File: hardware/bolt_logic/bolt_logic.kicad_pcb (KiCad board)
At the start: 2 copper layers, 289 x 112 mm, 16 parts, among them CN1 GM X1 48-way, CN2 B2B 2x20 2.54mm

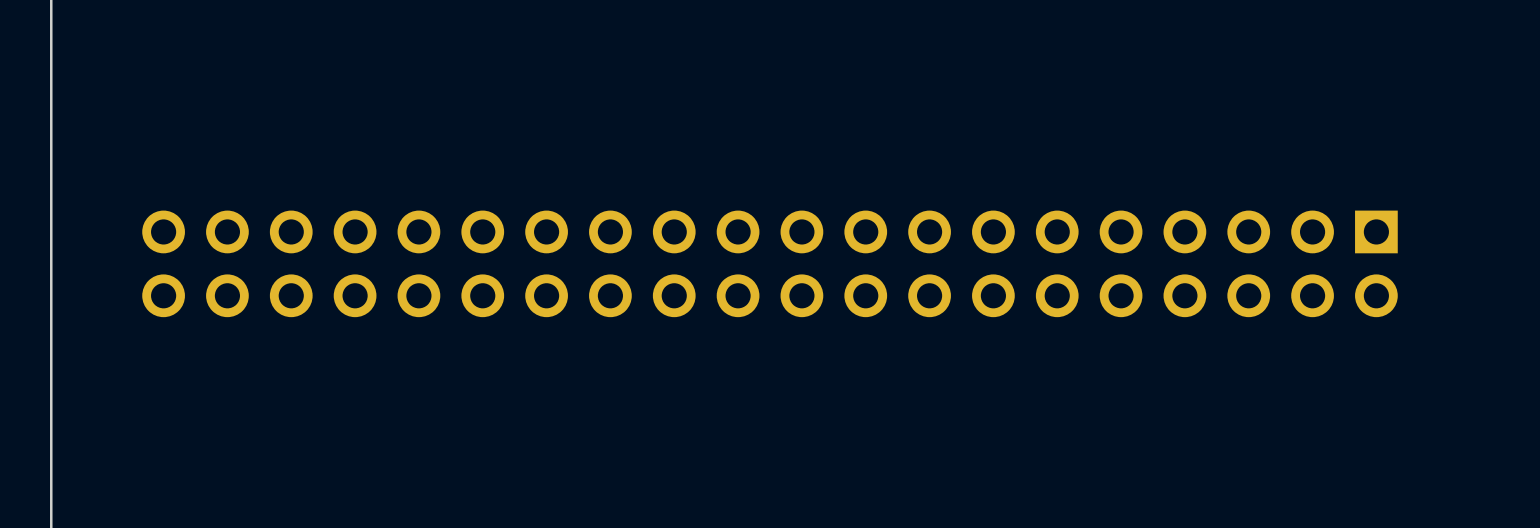
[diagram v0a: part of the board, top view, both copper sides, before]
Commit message: Add schematic design spec; identify CN2 as Samtec SSW-120-01-T-D-LL
docs/03-schematic-design.md: block-by-block design from a full read of the
Tesla V6 schematic - HW_BOLT STM32 pin map, reuse/adapt/new/drop per block
with values, CN1/CN2 net assignments, CN1 vehicle-pinout proposal,
software-resolver front end, firmware change list, open questions.

CN2 footprint: 1.02 mm drill for Samtec SSW (0.64 mm square tails).
Architecture doc corrected: the V6 hardware is encoder-only (resolver is
new design) and current gain is 2.25 digits/A with the V6's 2k7/4k7 divider.

Co-Authored-By: Claude Opus 5.5 <noreply@anthropic.com>
Claude-Session: https://claude.ai/code/session_01KW1M8KfVLc83FDDiK2YEWM
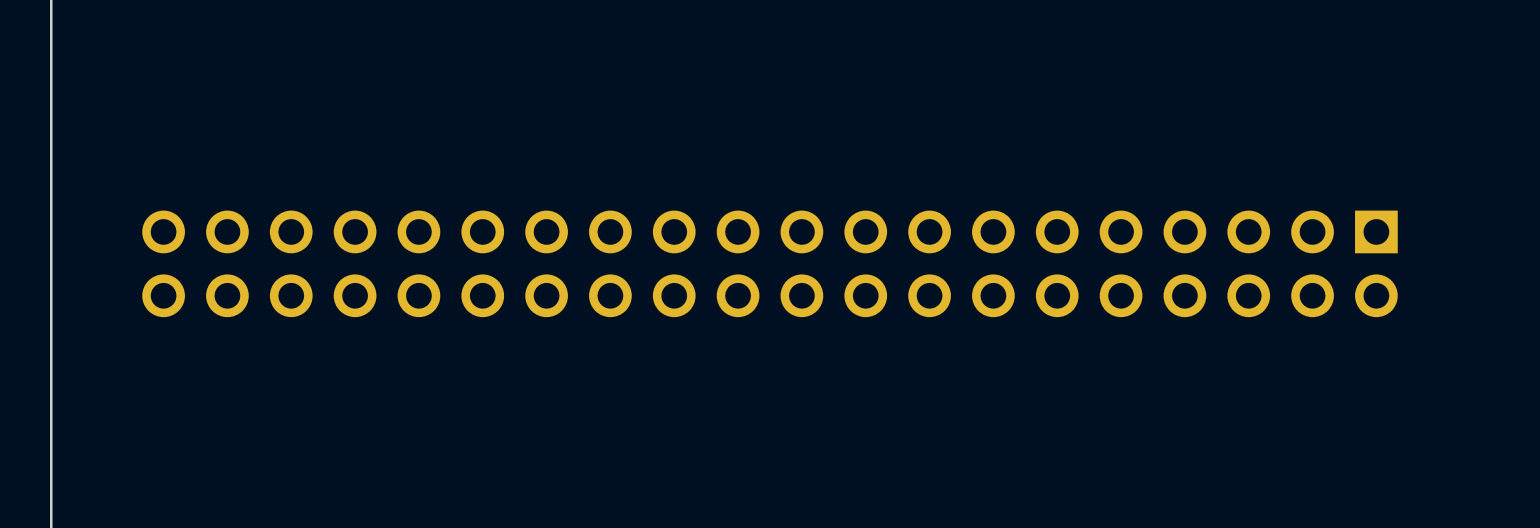
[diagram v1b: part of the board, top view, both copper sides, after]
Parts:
- CN2: value B2B 2x20 2.54mm -> SSW-120-01-T-D-LL

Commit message: PCB layout v0.1: scripted placement and autorouting, DRC clean
- gen_layout.py: footprints from the KiCad netlist with a pad-by-pad
  cross-check, grouped placement by function, decoupling caps placed at
  their pins, 2-pin parts rotated so each pad faces its own net.
- gen_route.py: 4-layer stackup (In1 solid GND), pre-routed short pad
  pairs, GND fan-out before routing, FreeRouting via DSN/SES with a
  custom SES importer (KiCad 7 import needs the GUI), dangling cleanup,
  direct completion of leftover connections, GND stitching, pours with
  orphan-island vias, DRC and a routed render.
- Net class widths are capped below the narrowest SMD pad on each net
  (FreeRouting cannot neck down into fine-pitch pins).
- Result: 0 clearance/short violations, 0 unconnected items; 17 silk
  warnings remain for the hand-review pass.
- gen_mech.py keeps footprint files unchanged when only tstamps differ.
- docs/04-layout.md: flow, results and the hand-review list before fab.

Co-Authored-By: Claude Opus 5.5 <noreply@anthropic.com>
Claude-Session: https://claude.ai/code/session_01KW1M8KfVLc83FDDiK2YEWM
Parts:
- added C1: 10uF 50V, Capacitor_SMD:C_1206_3216Metric, F.Cu at (85.2, 111.9)
- added C10: 10uF, Capacitor_SMD:C_1206_3216Metric, F.Cu at (105.1, 122.8)
- added C100: 1uF, Capacitor_SMD:C_0805_2012Metric, F.Cu at (137.2, 147.0)
- added C101: 1uF, Capacitor_SMD:C_0805_2012Metric, F.Cu at (140.3, 151.5)
- added C102: 1uF, Capacitor_SMD:C_0805_2012Metric, F.Cu at (98.8, 133.0)
- added C103: 1uF, Capacitor_SMD:C_0805_2012Metric, F.Cu at (140.3, 147.8)
- added C104: 1uF, Capacitor_SMD:C_0805_2012Metric, F.Cu at (130.5, 140.3)
- added C105: 100nF, Capacitor_SMD:C_0805_2012Metric, F.Cu at (150.0, 150.0)
- added C106: 100nF, Capacitor_SMD:C_0805_2012Metric, F.Cu at (145.5, 150.0)
- added C107: 1uF, Capacitor_SMD:C_0805_2012Metric, F.Cu at (107.0, 136.0)
- added C108: 1uF, Capacitor_SMD:C_0805_2012Metric, F.Cu at (135.0, 143.3)
- added C109: 100nF, Capacitor_SMD:C_0805_2012Metric, F.Cu at (82.7, 136.0)
- added C11: 22uF, Capacitor_SMD:C_1206_3216Metric, F.Cu at (105.1, 119.8)
- added C12: 100nF, Capacitor_SMD:C_0805_2012Metric, F.Cu at (106.0, 117.0)
- added C120: 10uF, Capacitor_SMD:C_1206_3216Metric, F.Cu at (325.4, 161.4)
- added C121: 100nF, Capacitor_SMD:C_0805_2012Metric, F.Cu at (328.2, 165.7)
- added C122: 100nF, Capacitor_SMD:C_0805_2012Metric, F.Cu at (321.5, 159.8)
- added C13: 10uF, Capacitor_SMD:C_1206_3216Metric, F.Cu at (98.3, 120.6)
- added C14: 100nF, Capacitor_SMD:C_0805_2012Metric, F.Cu at (94.8, 111.8)
- added C15: 10uF 25V, Capacitor_SMD:C_1206_3216Metric, F.Cu at (75.4, 105.2)
- added C16: 100nF, Capacitor_SMD:C_0805_2012Metric, F.Cu at (82.8, 104.3)
- added C2: 10uF 50V, Capacitor_SMD:C_1206_3216Metric, F.Cu at (88.2, 111.9)
- added C20: 100nF, Capacitor_SMD:C_0805_2012Metric, F.Cu at (145.5, 183.8)
- added C21: 100nF, Capacitor_SMD:C_0805_2012Metric, F.Cu at (152.3, 183.8)
- added C22: 100nF, Capacitor_SMD:C_0805_2012Metric, F.Cu at (159.7, 171.0)
- added C23: 100nF, Capacitor_SMD:C_0805_2012Metric, F.Cu at (139.5, 169.5)
- added C24: 4.7uF, Capacitor_SMD:C_0805_2012Metric, F.Cu at (136.5, 168.7)
- added C25: 1uF, Capacitor_SMD:C_0805_2012Metric, F.Cu at (139.5, 182.3)
- added C26: 100nF, Capacitor_SMD:C_0805_2012Metric, F.Cu at (136.5, 178.5)
- added C27: 100nF, Capacitor_SMD:C_0805_2012Metric, F.Cu at (142.5, 183.8)
- added C28: 22pF, Capacitor_SMD:C_0805_2012Metric, F.Cu at (132.0, 171.7)
- added C29: 22pF, Capacitor_SMD:C_0805_2012Metric, F.Cu at (132.0, 175.5)
- added C3: 10uF 50V, Capacitor_SMD:C_1206_3216Metric, F.Cu at (79.9, 105.2)
- added C30: 10pF, Capacitor_SMD:C_0805_2012Metric, F.Cu at (136.5, 181.5)
- added C31: 10pF, Capacitor_SMD:C_0805_2012Metric, F.Cu at (139.5, 186.0)
- added C4: 10uF 50V, Capacitor_SMD:C_1206_3216Metric, F.Cu at (84.1, 107.8)
- added C40: 100nF, Capacitor_SMD:C_0805_2012Metric, F.Cu at (106.7, 170.2)
- added C41: 10nF, Capacitor_SMD:C_0805_2012Metric, F.Cu at (109.0, 174.8)
- added C42: 10nF, Capacitor_SMD:C_0805_2012Metric, F.Cu at (110.5, 171.7)
- added C43: 10nF, Capacitor_SMD:C_0805_2012Metric, F.Cu at (102.2, 176.2)
- added C44: 10nF, Capacitor_SMD:C_0805_2012Metric, F.Cu at (106.0, 173.2)
- added C45: 10nF, Capacitor_SMD:C_0805_2012Metric, F.Cu at (111.0, 195.3)
- added C46: 100nF, Capacitor_SMD:C_0805_2012Metric, F.Cu at (110.5, 168.0)
- added C47: 100nF, Capacitor_SMD:C_0805_2012Metric, F.Cu at (110.5, 165.0)
- added C48: 1nF, Capacitor_SMD:C_0805_2012Metric, F.Cu at (124.8, 162.0)
- added C5: 100nF, Capacitor_SMD:C_0805_2012Metric, F.Cu at (91.7, 113.2)
- added C50: 4.7nF, Capacitor_SMD:C_0805_2012Metric, F.Cu at (80.8, 196.0)
- added C51: 1nF, Capacitor_SMD:C_0805_2012Metric, F.Cu at (75.5, 177.7)
- added C52: 4.7nF, Capacitor_SMD:C_0805_2012Metric, F.Cu at (84.5, 191.5)
- added C53: 1nF, Capacitor_SMD:C_0805_2012Metric, F.Cu at (75.5, 172.5)
- added C54: 100nF, Capacitor_SMD:C_0805_2012Metric, F.Cu at (74.8, 199.8)
- added C55: 4.7nF, Capacitor_SMD:C_0805_2012Metric, F.Cu at (69.5, 200.5)
- added C56: 1nF, Capacitor_SMD:C_0805_2012Metric, F.Cu at (71.0, 174.7)
- added C57: 100nF, Capacitor_SMD:C_0805_2012Metric, F.Cu at (66.5, 198.3)
- added C58: 1uF, Capacitor_SMD:C_0805_2012Metric, F.Cu at (89.0, 162.0)
- added C59: 1uF, Capacitor_SMD:C_0805_2012Metric, F.Cu at (83.0, 160.5)
- added C6: 100nF, Capacitor_SMD:C_0805_2012Metric, F.Cu at (94.0, 118.5)
- added C60: 100nF, Capacitor_SMD:C_0805_2012Metric, F.Cu at (69.5, 162.7)
- added C61: 100nF, Capacitor_SMD:C_0805_2012Metric, F.Cu at (67.2, 166.5)
- added C62: 100nF, Capacitor_SMD:C_0805_2012Metric, F.Cu at (88.3, 192.3)
- added C63: 1uF, Capacitor_SMD:C_0805_2012Metric, F.Cu at (71.7, 165.7)
- added C64: 1uF, Capacitor_SMD:C_0805_2012Metric, F.Cu at (69.5, 169.5)
- added C65: 1uF, Capacitor_SMD:C_0805_2012Metric, F.Cu at (71.8, 177.8)
- added C66: 1uF, Capacitor_SMD:C_0805_2012Metric, F.Cu at (78.5, 160.5)
- added C67: 1uF, Capacitor_SMD:C_0805_2012Metric, F.Cu at (74.0, 161.2)
- added C7: 22uF, Capacitor_SMD:C_1206_3216Metric, F.Cu at (96.1, 115.3)
- added C70: 3.3nF, Capacitor_SMD:C_0805_2012Metric, F.Cu at (111.3, 154.0)
- added C71: 4.7nF, Capacitor_SMD:C_0805_2012Metric, F.Cu at (88.0, 157.0)
- added C72: 2.2nF, Capacitor_SMD:C_0805_2012Metric, F.Cu at (95.5, 154.0)
- added C73: 100nF, Capacitor_SMD:C_0805_2012Metric, F.Cu at (76.0, 142.0)
- added C75: 100nF, Capacitor_SMD:C_0805_2012Metric, F.Cu at (103.7, 155.5)
- added C76: 1uF, Capacitor_SMD:C_0805_2012Metric, F.Cu at (94.8, 150.3)
- added C77: 10uF 25V, Capacitor_SMD:C_1206_3216Metric, F.Cu at (96.8, 144.1)
- added C78: 10uF 25V, Capacitor_SMD:C_1206_3216Metric, F.Cu at (98.3, 139.6)
- added C79: 100nF, Capacitor_SMD:C_0805_2012Metric, F.Cu at (103.0, 142.0)
- added C8: 22uF, Capacitor_SMD:C_1206_3216Metric, F.Cu at (91.2, 108.9)
- added C80: 10uF 25V, Capacitor_SMD:C_1206_3216Metric, F.Cu at (103.6, 138.8)
- added C81: 10uF 25V, Capacitor_SMD:C_1206_3216Metric, F.Cu at (97.9, 148.2)
- added C82: 1nF, Capacitor_SMD:C_0805_2012Metric, F.Cu at (75.2, 139.0)
- added C83: 1nF, Capacitor_SMD:C_0805_2012Metric, F.Cu at (96.2, 157.0)
- added C84: 100nF, Capacitor_SMD:C_0805_2012Metric, F.Cu at (105.2, 149.5)
- added C85: 1nF, Capacitor_SMD:C_0805_2012Metric, F.Cu at (99.2, 152.5)
- added C86: 1nF, Capacitor_SMD:C_0805_2012Metric, F.Cu at (100.0, 155.5)
- added C87: 1nF, Capacitor_SMD:C_0805_2012Metric, F.Cu at (101.5, 149.5)
- added C88: 1nF, Capacitor_SMD:C_0805_2012Metric, F.Cu at (101.5, 145.0)
- added C89: 1nF, Capacitor_SMD:C_0805_2012Metric, F.Cu at (103.0, 152.5)
- added C9: 100nF, Capacitor_SMD:C_0805_2012Metric, F.Cu at (88.0, 107.3)
- added D1: SS54, Diode_SMD:D_SMA, F.Cu at (77.8, 110.2)
- added D2: BAT54S, Package_TO_SOT_SMD:SOT-23, F.Cu at (124.2, 168.6)
- added F1: 50mA, Fuse:Fuse_1206_3216Metric, F.Cu at (95.1, 130.2)
- added F2: 200mA, Fuse:Fuse_1206_3216Metric, F.Cu at (96.3, 126.1)
- added F3: 100mA, Fuse:Fuse_1206_3216Metric, F.Cu at (101.6, 126.1)
- added F4: 500mA, Fuse:Fuse_1812_4532Metric, F.Cu at (208.7, 104.0)
- added FB1: 600R@100MHz 1A, Inductor_SMD:L_0805_2012Metric, F.Cu at (86.5, 123.1)
- added J1: SWD, Connector_PinHeader_2.54mm:PinHeader_1x05_P2.54mm_Vertical, F.Cu at (145.6, 165.7)
- added J3: AUX I/O, Connector_PinHeader_2.54mm:PinHeader_2x06_P2.54mm_Vertical, F.Cu at (201.8, 101.5)
- added J4: ESP PROG, Connector_PinHeader_2.54mm:PinHeader_1x06_P2.54mm_Vertical, F.Cu at (307.3, 185.9)
- added L1: 6.8uH, Inductor_SMD:L_Bourns_SRN6045TA, F.Cu at (88.8, 118.2)
- added L2: 10uH, Inductor_SMD:L_0805_2012Metric, F.Cu at (139.4, 174.0)
- added L30: 10uH, Inductor_SMD:L_0805_2012Metric, F.Cu at (293.8, 167.4)
- added LED1: PWR green, LED_SMD:LED_0805_2012Metric, F.Cu at (156.8, 176.3)
- added LED2: STATUS, LED_SMD:LED_0805_2012Metric, F.Cu at (150.0, 161.3)
- added Q1: BTS443P, Package_TO_SOT_SMD:TO-252-4, F.Cu at (69.5, 117.6)
- added Q2: BTS443P, Package_TO_SOT_SMD:TO-252-4, F.Cu at (77.0, 117.6)
- added R1: 10k, Resistor_SMD:R_0805_2012Metric, F.Cu at (67.0, 110.3)
- added R10: 10k, Resistor_SMD:R_0805_2012Metric, F.Cu at (141.7, 166.5)
- added R100: 4.7k, Resistor_SMD:R_0805_2012Metric, F.Cu at (129.7, 153.0)
- added R101: 1.5k, Resistor_SMD:R_0805_2012Metric, F.Cu at (130.5, 150.0)
- added R102: 4.7k, Resistor_SMD:R_0805_2012Metric, F.Cu at (133.5, 153.0)
- added R103: 1.5k, Resistor_SMD:R_0805_2012Metric, F.Cu at (134.2, 150.0)
- added R104: 4.7k, Resistor_SMD:R_0805_2012Metric, F.Cu at (95.7, 136.0)
- added R105: 1.5k, Resistor_SMD:R_0805_2012Metric, F.Cu at (99.5, 136.0)
- added R106: 4.7k, Resistor_SMD:R_0805_2012Metric, F.Cu at (137.2, 153.0)
- added R107: 1.5k, Resistor_SMD:R_0805_2012Metric, F.Cu at (138.0, 150.0)
- added R108: 4.7k, Resistor_SMD:R_0805_2012Metric, F.Cu at (129.7, 147.0)
- added R109: 1.5k, Resistor_SMD:R_0805_2012Metric, F.Cu at (130.5, 144.0)
- added R11: 4.7k, Resistor_SMD:R_0805_2012Metric, F.Cu at (150.0, 183.8)
- added R110: 1k, Resistor_SMD:R_0805_2012Metric, F.Cu at (153.0, 152.3)
- added R111: 10k, Resistor_SMD:R_0805_2012Metric, F.Cu at (150.0, 153.0)
- added R112: 1k, Resistor_SMD:R_0805_2012Metric, F.Cu at (143.2, 152.3)
- added R113: 10k, Resistor_SMD:R_0805_2012Metric, F.Cu at (146.2, 153.0)
- added R114: 10k, Resistor_SMD:R_0805_2012Metric, F.Cu at (103.2, 136.0)
- added R115: 10k, Resistor_SMD:R_0805_2012Metric, F.Cu at (102.5, 133.0)
- added R116: 10k, Resistor_SMD:R_0805_2012Metric, F.Cu at (133.5, 147.0)
- added R117: 10k, Resistor_SMD:R_0805_2012Metric, F.Cu at (132.7, 144.0)
- added R12: 470, Resistor_SMD:R_0805_2012Metric, F.Cu at (156.7, 171.8)
- added R120: 10k, Resistor_SMD:R_0805_2012Metric, F.Cu at (130.0, 99.0)
- added R121: 10k, Resistor_SMD:R_0805_2012Metric, F.Cu at (142.0, 99.0)
- added R122: 10k, Resistor_SMD:R_0805_2012Metric, F.Cu at (163.7, 114.8)
- added R123: 120, Resistor_SMD:R_0805_2012Metric, F.Cu at (77.5, 127.0)
- added R124: 0R, Resistor_SMD:R_0805_2012Metric, F.Cu at (80.5, 127.0)
- added R13: 1k, Resistor_SMD:R_0805_2012Metric, F.Cu at (147.7, 161.3)
- added R130: 4.7k, Resistor_SMD:R_0805_2012Metric, F.Cu at (322.2, 162.8)
- added R14: 10k, Resistor_SMD:R_0805_2012Metric, F.Cu at (142.5, 163.5)
- added R2: 6.8k, Resistor_SMD:R_0805_2012Metric, F.Cu at (67.0, 106.5)
- added R20: 124k, Resistor_SMD:R_0805_2012Metric, F.Cu at (97.0, 164.3)
- added R21: 100k, Resistor_SMD:R_0805_2012Metric, F.Cu at (97.7, 180.0)
- added R22: 560, Resistor_SMD:R_0805_2012Metric, F.Cu at (106.0, 175.5)
- added R23: 100k, Resistor_SMD:R_0805_2012Metric, F.Cu at (100.7, 179.3)
- added R24: 560, Resistor_SMD:R_0805_2012Metric, F.Cu at (109.0, 180.0)
- added R25: 100k, Resistor_SMD:R_0805_2012Metric, F.Cu at (105.7, 191.5)
- added R26: 560, Resistor_SMD:R_0805_2012Metric, F.Cu at (105.2, 180.0)
- added R27: 100k, Resistor_SMD:R_0805_2012Metric, F.Cu at (97.7, 177.0)
- added R28: 560, Resistor_SMD:R_0805_2012Metric, F.Cu at (106.7, 177.8)
- added R29: 100k, Resistor_SMD:R_0805_2012Metric, F.Cu at (105.7, 193.8)
- added R3: 1k, Resistor_SMD:R_0805_2012Metric, F.Cu at (82.7, 122.3)
- added R30: 560, Resistor_SMD:R_0805_2012Metric, F.Cu at (108.7, 192.3)
- added R31: 10k, Resistor_SMD:R_0805_2012Metric, F.Cu at (122.5, 179.3)
- added R32: 20k, Resistor_SMD:R_0805_2012Metric, F.Cu at (123.2, 176.3)
- added R33: 1k, Resistor_SMD:R_0805_2012Metric, F.Cu at (124.0, 172.5)
- added R34: 33k, Resistor_SMD:R_0805_2012Metric, F.Cu at (102.2, 173.3)
- added R35: 10k, Resistor_SMD:R_0805_2012Metric, F.Cu at (103.0, 170.3)
- added R36: 3.3k, Resistor_SMD:R_0805_2012Metric, F.Cu at (124.0, 165.0)
- added R37: 10k, Resistor_SMD:R_0805_2012Metric, F.Cu at (97.7, 174.0)
- added R4: 1k, Resistor_SMD:R_0805_2012Metric, F.Cu at (91.0, 123.0)
- added R40: 1k, Resistor_SMD:R_0805_2012Metric, F.Cu at (80.7, 192.3)
- added R41: 2.7k, Resistor_SMD:R_0805_2012Metric, F.Cu at (83.0, 179.3)
- added R42: 4.7k, Resistor_SMD:R_0805_2012Metric, F.Cu at (80.0, 178.5)
- added R43: 1k, Resistor_SMD:R_0805_2012Metric, F.Cu at (76.2, 180.0)
- added R44: 2.7k, Resistor_SMD:R_0805_2012Metric, F.Cu at (83.0, 176.3)
- added R45: 4.7k, Resistor_SMD:R_0805_2012Metric, F.Cu at (83.0, 174.0)
- added R46: 1k, Resistor_SMD:R_0805_2012Metric, F.Cu at (70.2, 197.5)
- added R47: 2.7k, Resistor_SMD:R_0805_2012Metric, F.Cu at (79.2, 175.5)
- added R48: 4.7k, Resistor_SMD:R_0805_2012Metric, F.Cu at (76.2, 174.8)
- added R49: 10k, Resistor_SMD:R_0805_2012Metric, F.Cu at (93.5, 162.0)
- added R5: 10k, Resistor_SMD:R_0805_2012Metric, F.Cu at (94.7, 123.0)
- added R50: 10k, Resistor_SMD:R_0805_2012Metric, F.Cu at (85.2, 162.8)
- added R51: 10k, Resistor_SMD:R_0805_2012Metric, F.Cu at (76.2, 168.8)
- added R52: 4.7k, Resistor_SMD:R_0805_2012Metric, F.Cu at (76.2, 165.8)
- added R53: 4.7k, Resistor_SMD:R_0805_2012Metric, F.Cu at (73.2, 168.8)
- added R54: 4.7k, Resistor_SMD:R_0805_2012Metric, F.Cu at (71.7, 171.8)
- added R55: 2.2k, Resistor_SMD:R_0805_2012Metric, F.Cu at (81.5, 162.8)
- added R56: 2.2k, Resistor_SMD:R_0805_2012Metric, F.Cu at (76.2, 163.5)
- added R6: 1k, Resistor_SMD:R_0805_2012Metric, F.Cu at (82.0, 114.8)
- added R60: 0R, Resistor_SMD:R_0805_2012Metric, F.Cu at (118.0, 157.0)
- added R61: 10k, Resistor_SMD:R_0805_2012Metric, F.Cu at (114.2, 157.0)
- added R62: 10k, Resistor_SMD:R_0805_2012Metric, F.Cu at (110.5, 157.0)
- added R63: 10k, Resistor_SMD:R_0805_2012Metric, F.Cu at (92.5, 156.3)
- added R64: 10k, Resistor_SMD:R_0805_2012Metric, F.Cu at (78.2, 151.0)
- added R65: 10k, Resistor_SMD:R_0805_2012Metric, F.Cu at (77.5, 148.0)
- added R67: 10k, Resistor_SMD:R_0805_2012Metric, F.Cu at (91.0, 142.8)
- added R68: 10k, Resistor_SMD:R_0805_2012Metric, F.Cu at (91.0, 146.5)
- added R69: 100k, Resistor_SMD:R_0805_2012Metric, F.Cu at (93.2, 142.8)
- added R7: 0R, Resistor_SMD:R_1206_3216Metric, F.Cu at (68.3, 98.1)
- added R70: 20k, Resistor_SMD:R_0805_2012Metric, F.Cu at (91.0, 139.0)
- added R71: 10k, Resistor_SMD:R_0805_2012Metric, F.Cu at (94.0, 139.8)
- added R72: 10k, Resistor_SMD:R_0805_2012Metric, F.Cu at (79.7, 142.8)
- added R73: 10k, Resistor_SMD:R_0805_2012Metric, F.Cu at (79.7, 139.8)
- added R74: 10, Resistor_SMD:R_1206_3216Metric, F.Cu at (68.3, 150.9)
- added R75: 10, Resistor_SMD:R_1206_3216Metric, F.Cu at (73.6, 147.9)
- added R76: 10k, Resistor_SMD:R_0805_2012Metric, F.Cu at (73.0, 151.0)
- added R77: 10k, Resistor_SMD:R_0805_2012Metric, F.Cu at (67.7, 148.0)
- added R78: 4.7k, Resistor_SMD:R_0805_2012Metric, F.Cu at (81.2, 150.3)
- added R79: 4.7k, Resistor_SMD:R_0805_2012Metric, F.Cu at (73.0, 145.0)
- added R80: 10k, Resistor_SMD:R_0805_2012Metric, F.Cu at (67.7, 145.8)
- added R81: 10k, Resistor_SMD:R_0805_2012Metric, F.Cu at (67.7, 143.5)
- added R82: 4.7k, Resistor_SMD:R_0805_2012Metric, F.Cu at (84.2, 155.5)
- added R83: 4.7k, Resistor_SMD:R_0805_2012Metric, F.Cu at (71.5, 142.8)
- added R84: 100, Resistor_SMD:R_0805_2012Metric, F.Cu at (85.0, 149.5)
- added R85: 0R, Resistor_SMD:R_0805_2012Metric, F.Cu at (91.7, 151.8)
- added R86: 100, Resistor_SMD:R_0805_2012Metric, F.Cu at (85.0, 152.5)
- added R87: 0R, Resistor_SMD:R_0805_2012Metric, F.Cu at (90.2, 154.0)
- added R88: 10k, Resistor_SMD:R_0805_2012Metric, F.Cu at (67.7, 138.3)
- added R89: 0R (DNP), Resistor_SMD:R_0805_2012Metric, F.Cu at (88.7, 149.5)
- added R90: 10k, Resistor_SMD:R_0805_2012Metric, F.Cu at (67.7, 140.5)
- added R91: 0R (DNP), Resistor_SMD:R_0805_2012Metric, F.Cu at (76.7, 145.0)
- added R92: 10k, Resistor_SMD:R_0805_2012Metric, F.Cu at (71.5, 138.3)
- added R93: 0R (DNP), Resistor_SMD:R_0805_2012Metric, F.Cu at (94.0, 147.3)
- added RN1: 4x10k, Resistor_SMD:R_Array_Convex_4x0603, F.Cu at (114.9, 195.4)
- added RN2: 4x10k, Resistor_SMD:R_Array_Convex_4x0603, F.Cu at (119.4, 195.4)
- added TP1: GB_AUX, TestPoint:TestPoint_Pad_D1.5mm, F.Cu at (97.3, 171.5)
- added TP2: GB_UDC, TestPoint:TestPoint_Pad_D1.5mm, F.Cu at (100.3, 170.7)
- added TVS1: SMBJ26CA, Diode_SMD:D_SMB, F.Cu at (71.3, 108.3)
- added U1: AP63205WU, Package_TO_SOT_SMD:TSOT-23-6, F.Cu at (83.1, 119.3)
- added U10: LM2901, Package_SO:SOIC-14_3.9x8.7mm_P1.27mm, F.Cu at (83.0, 168.3)
- added U11: 74HCT4052, Package_SO:SOIC-16_3.9x9.9mm_P1.27mm, F.Cu at (90.4, 177.3)
- added U12: MCP6292, Package_SO:SOIC-8_3.9x4.9mm_P1.27mm, F.Cu at (69.7, 155.3)
- added U13: L272D, Package_SO:SOIC-16_3.9x9.9mm_P1.27mm, F.Cu at (85.5, 143.0)
- added U14: MCP6292, Package_SO:SOIC-8_3.9x4.9mm_P1.27mm, F.Cu at (78.7, 155.3)
- added U2: LD1117S33TR, Package_TO_SOT_SMD:SOT-223-3_TabPin2, F.Cu at (112.4, 120.4)
- added U20: BTS133TC, Package_TO_SOT_SMD:TO-263-2, F.Cu at (131.7, 107.8)
- added U21: BTS133TC, Package_TO_SOT_SMD:TO-263-2, F.Cu at (143.7, 107.8)
- added U22: BTS133TC, Package_TO_SOT_SMD:TO-263-2, F.Cu at (155.7, 107.8)
- added U23: SN65HVD234, Package_SO:SOIC-8_3.9x4.9mm_P1.27mm, F.Cu at (77.9, 133.3)
- added U3: STM32F103RBT6, Package_QFP:LQFP-64_10x10mm_P0.5mm, F.Cu at (148.0, 175.0)
- added U30: ESP32-WROOM-32UE, RF_Module:ESP32-WROOM-32UE, F.Cu at (316.0, 174.0)
- added U4: 74HCT573, Package_SO:SOIC-20W_7.5x12.8mm_P1.27mm, F.Cu at (117.6, 187.3)
- added U5: 74HC21, Package_SO:SOIC-14_3.9x8.7mm_P1.27mm, F.Cu at (115.8, 177.3)
- added U6: CD74HCT30, Package_SO:SOIC-14_3.9x8.7mm_P1.27mm, F.Cu at (117.3, 169.0)
- added U7: MCP6292, Package_SO:SOIC-8_3.9x4.9mm_P1.27mm, F.Cu at (76.6, 194.0)
- added U8: MCP6292, Package_SO:SOIC-8_3.9x4.9mm_P1.27mm, F.Cu at (69.2, 193.5)
- added U9: LM2901, Package_SO:SOIC-14_3.9x8.7mm_P1.27mm, F.Cu at (91.7, 168.1)
- added Y1: 8MHz, Crystal:Crystal_SMD_5032-2Pin_5.0x3.2mm, F.Cu at (135.9, 173.4)
- added Y2: 32.768kHz, Crystal:Crystal_SMD_3215-2Pin_3.2x1.5mm, F.Cu at (139.7, 178.2)
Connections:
- CN1 pad A1: (no net) -> THR1_IN
- CN1 pad A2: (no net) -> THR2_IN
- CN1 pad A3: (no net) -> PEDAL_5V
- CN1 pad A4: (no net) -> GND
- CN1 pad B1: (no net) -> EXC_N
- CN1 pad B2: (no net) -> EXC_P
- CN1 pad B3: (no net) -> PUMP_OUT_SW
- CN1 pad B4: (no net) -> FWD_12V
- CN1 pad C1: (no net) -> SIN_N
- CN1 pad C2: (no net) -> SIN_P
- CN1 pad C3: (no net) -> REV_12V
- CN1 pad C4: (no net) -> BRAKE_12V
- CN1 pad D1: (no net) -> COS_N
- CN1 pad D2: (no net) -> COS_P
- CN1 pad D3: (no net) -> START_12V
- CN1 pad D4: (no net) -> CRUISE_12V
- CN1 pad E1: (no net) -> MAIN_CONT_OUT
- CN1 pad E2: (no net) -> PRECHG_OUT_SW
- CN1 pad E3: (no net) -> CAN_L
- CN1 pad E4: (no net) -> CAN_H
- CN1 pad F3: (no net) -> CAN_L
- CN1 pad F4: (no net) -> CAN_H
- CN1 pad G1: (no net) -> HVIL_REF
- CN1 pad G2: (no net) -> HVIL_SIG
- CN1 pad J1: (no net) -> MOT_TEMP
- CN1 pad J2: (no net) -> GND
- CN1 pad K1: (no net) -> ENC_A_IN
- CN1 pad K2: (no net) -> GND
- CN1 pad K3: (no net) -> ENC_B_IN
- CN1 pad K4: (no net) -> ENC_Z_IN
- CN1 pad L2: (no net) -> ENC_5V
- CN1 pad L3: (no net) -> IGN
- CN1 pad M1: (no net) -> VBAT
- CN1 pad M3: (no net) -> GND
- CN1 pad M4: (no net) -> VBAT
- CN2 pad 1: (no net) -> GND
- CN2 pad 10: (no net) -> HEALTH4
- CN2 pad 11: (no net) -> GB_PWM_UH
- CN2 pad 12: (no net) -> GB_PWM_UL
- CN2 pad 13: (no net) -> GB_PWM_VH
- CN2 pad 14: (no net) -> GB_PWM_VL
- CN2 pad 15: (no net) -> GB_PWM_WH
- CN2 pad 16: (no net) -> GB_PWM_WL
- CN2 pad 17: (no net) -> NTC_U
- CN2 pad 18: (no net) -> GB_UDC
- CN2 pad 19: (no net) -> NTC_V
- CN2 pad 2: (no net) -> GND
- CN2 pad 20: (no net) -> GB_AUX
- CN2 pad 21: (no net) -> NTC_W
- CN2 pad 22: (no net) -> GATE_FLT
- CN2 pad 23: (no net) -> GND
- CN2 pad 24: (no net) -> ISNS_U
- CN2 pad 25: (no net) -> GND
- CN2 pad 26: (no net) -> ISNS_W
- CN2 pad 27: (no net) -> ISNS_V
- CN2 pad 28: (no net) -> +5V_A
- CN2 pad 29: (no net) -> +5V_A
- CN2 pad 3: (no net) -> +5V
- CN2 pad 30: (no net) -> GND
- CN2 pad 31: (no net) -> +12V_GATE
- CN2 pad 32: (no net) -> GND
- CN2 pad 33: (no net) -> +12V_GATE
- CN2 pad 34: (no net) -> GND
- CN2 pad 35: (no net) -> +12V_GATE
- CN2 pad 36: (no net) -> IGN_SENSE
- CN2 pad 37: (no net) -> +12V_GATE
- CN2 pad 38: (no net) -> IGN_SENSE
- CN2 pad 39: (no net) -> GND
- CN2 pad 4: (no net) -> +5V
- CN2 pad 40: (no net) -> GND
- CN2 pad 5: (no net) -> GND
- CN2 pad 6: (no net) -> GND
- CN2 pad 7: (no net) -> HEALTH1
- CN2 pad 8: (no net) -> HEALTH2
- CN2 pad 9: (no net) -> HEALTH3
- H1 pad 1: (no net) -> CHASSIS
- H10 pad 1: (no net) -> CHASSIS
- H11 pad 1: (no net) -> CHASSIS
- H12 pad 1: (no net) -> CHASSIS
- H2 pad 1: (no net) -> CHASSIS
- H3 pad 1: (no net) -> CHASSIS
- H4 pad 1: (no net) -> CHASSIS
- H5 pad 1: (no net) -> CHASSIS
- H6 pad 1: (no net) -> CHASSIS
- H7 pad 1: (no net) -> CHASSIS
- H8 pad 1: (no net) -> CHASSIS
- H9 pad 1: (no net) -> CHASSIS
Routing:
- net CHASSIS: track 0.00 -> 652.8 mm, vias 0 -> 3
- net +5V: track 0.00 -> 473.4 mm, vias 0 -> 16
- net +3V3: track 0.00 -> 421.7 mm, vias 0 -> 6
- net GND: track 0.00 -> 236.3 mm, vias 0 -> 543
- net USART_RX: track 0.00 -> 181.8 mm, vias 0 -> 2
- net USART_TX: track 0.00 -> 181.0 mm, vias 0 -> 2
- net AUX_TEMP: track 0.00 -> 168.2 mm, vias 0 -> 3
- net VBAT_SW: track 0.00 -> 161.8 mm, vias 0 -> 2
- net HVIL_SIG: track 0.00 -> 161.6 mm, vias 0 -> 1
- net HVIL_REF: track 0.00 -> 156.3 mm, vias 0 -> 1
- net PRECHG_OUT_SW: track 0.00 -> 153.6 mm, vias 0 -> 3
- net PUMP_OUT_SW: track 0.00 -> 153.6 mm, vias 0 -> 4
- net +12V_GATE: track 0.00 -> 130.4 mm, vias 0 -> 3
- net +5V_A: track 0.00 -> 130.2 mm, vias 0 -> 3
- net AUX_5V: track 0.00 -> 109.0 mm, vias 0 -> 1
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- added copper zone on B.Cu, net GND
- added copper zone on F.Cu, net GND
- added copper zone on In1.Cu, net GND
- added copper zone on In2.Cu, net GND
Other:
- copper layers 2 -> 4

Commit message: Layout: V6 WiFi module at the bottom edge, height check, rip-up completion
- ESP32-WROOM-32E placed with its antenna end flush with the bottom board
  edge between H5 and H11 (the only edge stretch without a mounting hole
  for the 48 mm antenna keep-out); keep-out extended to all four copper
  layers and honoured by placement, routing, vias and pours.
- Height check in gen_layout.py: owner's ~7/8 in limit from the board
  bottom (20.2 mm above the component side); every footprint checked.
- Leftover connections: grid A* search through vias, then rip-up and
  reroute of crossed tracks; dangling vias cleaned up as well.
- FreeRouting second pass off by default (reproducible hang).
- DRC: 0 violations, 0 unconnected items.

Co-Authored-By: Claude Opus 5.5 <noreply@anthropic.com>
Claude-Session: https://claude.ai/code/session_01KW1M8KfVLc83FDDiK2YEWM
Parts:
- U30: value ESP32-WROOM-32UE -> ESP32-WROOM-32E; footprint RF_Module:ESP32-WROOM-32UE -> RF_Module:ESP32-WROOM-32
- moved R130 45.1 mm to (291.2, 195.5), turned to 90 degrees
- moved C122 44.0 mm to (291.3, 191.8)
- moved C121 43.5 mm to (296.5, 195.5)
- moved C120 43.0 mm to (295.6, 192.3), turned to 0 degrees
- moved J4 39.5 mm to (268.1, 181.2), turned to 0 degrees
- moved U30 39.1 mm to (280.0, 189.2), turned to 180 degrees
- moved L30 28.9 mm to (293.4, 196.2), turned to -90 degrees
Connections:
- C121 pad 1: ESP_3V3 -> +3V3
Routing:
- net USART_RX: track 181.8 -> 129.8 mm
- net USART_TX: track 181.0 -> 130.2 mm, vias 2 -> 1
- net START_IN: track 66.3 -> 37.3 mm, vias 2 -> 3
- net PRECHG_OUT_SW: track 153.6 -> 125.3 mm, vias 3 -> 2
- net NRST: track 61.1 -> 34.3 mm, vias 4 -> 2
- net +5V: track 473.4 -> 448.6 mm, vias 16 -> 13
- net VTG_OUT: track 84.0 -> 105.6 mm
- net +3V3: track 421.7 -> 441.7 mm, vias 6 -> 11
- net ESP_3V3: track 38.1 -> 19.7 mm
- net +12V_GATE: track 130.4 -> 112.6 mm
- net OCUR_OK: track 103.6 -> 87.1 mm
- net AUX_TEMP: track 168.2 -> 184.1 mm
- net THR1_IN: track 57.2 -> 72.4 mm, vias 1 -> 4
- net TMPM: track 67.7 -> 55.4 mm, vias 3 -> 2
- net GATE_FLT_F: track 32.0 -> 19.7 mm, vias 3 -> 2
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
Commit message: Layout: spread placement over the board, 10 mm CN1/CN2 clearance
- Placement regions now cover the whole board; MCU at the board centre.
- Owner: no component within 10 mm of CN1 or CN2 (hand soldering);
  enforced as a placement keep-out and checked after placement.
- Placement boxes include each part's silkscreen reference with 1.5 mm
  between boxes, so references are legible and back on the silkscreen
  (fab-layer move removed). DRC silkscreen overlaps: 17 -> 0.
- FreeRouting passes 100 -> 40 (long tails only made runs slower; the
  completion step closes what is left).
- DRC: 0 violations, 0 unconnected items.

Co-Authored-By: Claude Opus 5.5 <noreply@anthropic.com>
Claude-Session: https://claude.ai/code/session_01KW1M8KfVLc83FDDiK2YEWM
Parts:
- moved F3 98.0 mm to (199.6, 123.6)
- moved F2 96.1 mm to (192.4, 124.7), turned to -90 degrees
- moved U12 93.8 mm to (158.7, 125.8), turned to 90 degrees
- moved F1 92.0 mm to (186.8, 122.9), turned to 0 degrees
- moved R64 78.6 mm to (151.7, 123.3), turned to 90 degrees
- moved C107 78.5 mm to (185.1, 128.2)
- moved R49 77.2 mm to (170.5, 166.8), turned to 90 degrees
- moved R115 76.7 mm to (179.1, 128.3), turned to 0 degrees
- moved U9 76.1 mm to (167.4, 159.5), turned to 90 degrees
- moved R114 75.9 mm to (179.1, 133.5)
- moved R105 75.1 mm to (174.6, 138.8)
- moved R51 74.7 mm to (149.5, 154.0)
- moved C102 74.5 mm to (173.1, 128.2), turned to 0 degrees
- moved U10 73.6 mm to (156.0, 158.6), turned to 0 degrees
- moved R104 72.9 mm to (168.6, 138.8)
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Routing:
- net ENC_5V: track 40.4 -> 140.5 mm
- net PEDAL_5V: track 67.7 -> 163.0 mm, vias 1 -> 2
- net NTC_V: track 33.0 -> 121.2 mm
- net BRAKE_12V: track 55.9 -> 140.9 mm, vias 3 -> 2
- net THR1_IN: track 72.4 -> 153.9 mm, vias 4 -> 2
- net GB_AUX: track 22.7 -> 89.0 mm
- net MOT_TEMP: track 76.3 -> 141.9 mm
- net PUMP_OUT_SW: track 164.7 -> 228.2 mm
- net HVIL_REF: track 153.0 -> 216.0 mm, vias 1 -> 2
- net NTC_W: track 30.9 -> 91.8 mm
- net CHASSIS: track 646.3 -> 706.8 mm, vias 5 -> 2
- net GB_UDC: track 23.3 -> 83.5 mm
- net THR2_IN: track 85.7 -> 145.0 mm, vias 1 -> 2
- net IGN: track 98.2 -> 154.5 mm, vias 3 -> 2
- net POS_A: track 75.8 -> 131.9 mm, vias 2 -> 3
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
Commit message: Remove the aux header (J3) and V6 leftovers: only CN1, CN2 and programming
Owner: the only connections on the board are CN1, CN2 and what is needed
to program it (J1 SWD, J4 ESP32).

- Removed J3 and what only served it: aux 12 V / 5 V outputs (F3, F4),
  aux temperature pull-up and filter (R56, C67; mux 1Y1 grounded), the
  emergency-stop / motor-protection header resistors and caps (R110,
  R112, C105, C106; the 10k pull-ups stay, so the firmware reads OK).
- CN1 G1/G2 (HVIL) only went to J3: now reserved positions.
- PC11 (VTG_OUT) and PC5 (SPEED_OUT, never connected) now NC.
- Re-placed and re-routed: 241 parts, DRC 0 violations, 0 unconnected.
- Docs: 03 (pin map, 4.10, 4.12, 4.13, CN1 table), 04, 05 updated;
  SWD header described as the 5-pin part it is.

Co-Authored-By: Claude Opus 5.5 <noreply@anthropic.com>
Claude-Session: https://claude.ai/code/session_01KW1M8KfVLc83FDDiK2YEWM
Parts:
- removed C105, C106: 100nF, Capacitor_SMD:C_0805_2012Metric
- removed C67: 1uF, Capacitor_SMD:C_0805_2012Metric
- removed F3: 100mA, Fuse:Fuse_1206_3216Metric
- removed F4: 500mA, Fuse:Fuse_1812_4532Metric
- removed J3: AUX I/O, Connector_PinHeader_2.54mm:PinHeader_2x06_P2.54mm_Vertical
- removed R110, R112: 1k, Resistor_SMD:R_0805_2012Metric
- removed R56: 2.2k, Resistor_SMD:R_0805_2012Metric
- moved C107 17.1 mm to (198.6, 138.7)
- moved R114 17.1 mm to (192.6, 144.0)
- moved R115 17.1 mm to (192.6, 138.8)
- moved R116 13.1 mm to (179.1, 133.5)
- moved C60 11.8 mm to (135.2, 166.0), turned to 180 degrees
- moved R117 11.7 mm to (179.1, 128.3)
- moved C104 7.55 mm to (168.3, 127.2), turned to 90 degrees
- moved C61 7.42 mm to (130.0, 166.0)
- moved C103 6.45 mm to (187.3, 128.2)
- moved R113 6.45 mm to (200.8, 144.0)
- moved C65 6.42 mm to (139.8, 169.8), turned to -90 degrees
- moved C62 5.85 mm to (128.5, 161.5), turned to 90 degrees
- moved C101 5.46 mm to (191.1, 133.5)
- moved R111 3.59 mm to (206.8, 144.0), turned to 0 degrees
- moved C66 3.00 mm to (133.0, 160.7)
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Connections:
- CN1 pad G1: HVIL_REF -> (no net)
- CN1 pad G2: HVIL_SIG -> (no net)
- U11 pad 14: AUX_TEMP -> GND
- U3 pad 25: SPEED_OUT -> (no net)
- U3 pad 52: VTG_OUT -> (no net)
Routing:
- net HVIL_SIG: track 221.2 -> 0.00 mm, vias 2 -> 0
- net HVIL_REF: track 216.0 -> 0.00 mm, vias 2 -> 0
- net VBAT_SW: track 208.9 -> 31.0 mm, vias 3 -> 0
- net AUX_TEMP: track 170.4 -> 0.00 mm, vias 4 -> 0
- net MPROT_HDR: track 79.0 -> 0.00 mm
- net VTG_OUT: track 77.1 -> 0.00 mm, vias 2 -> 0
- net EMCYSTOP_HDR: track 67.5 -> 0.00 mm, vias 1 -> 0
- net AUX_5V: track 63.2 -> 0.00 mm
- net CHASSIS: track 706.8 -> 659.1 mm, vias 2 -> 3
- net ENC_5V: track 140.5 -> 167.2 mm
- net PEDAL_5V: track 163.0 -> 188.4 mm, vias 2 -> 1
- net MOT_TEMP: track 141.9 -> 119.3 mm, vias 3 -> 4
- net +3V3: track 443.9 -> 461.0 mm, vias 5 -> 12
- net BRAKE_IN: track 94.0 -> 78.5 mm
- net PUMP_OUT_SW: track 228.2 -> 212.8 mm, vias 1 -> 2
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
